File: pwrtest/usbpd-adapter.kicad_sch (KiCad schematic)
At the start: 30 parts, among them J1 Conn_01x04, J2 Conn_01x04, J3 USB_C_Receptacle_USB2.0_16P, Q1 AO3400A, U1 AP63205WU, U2 L7812, U3 IP2721

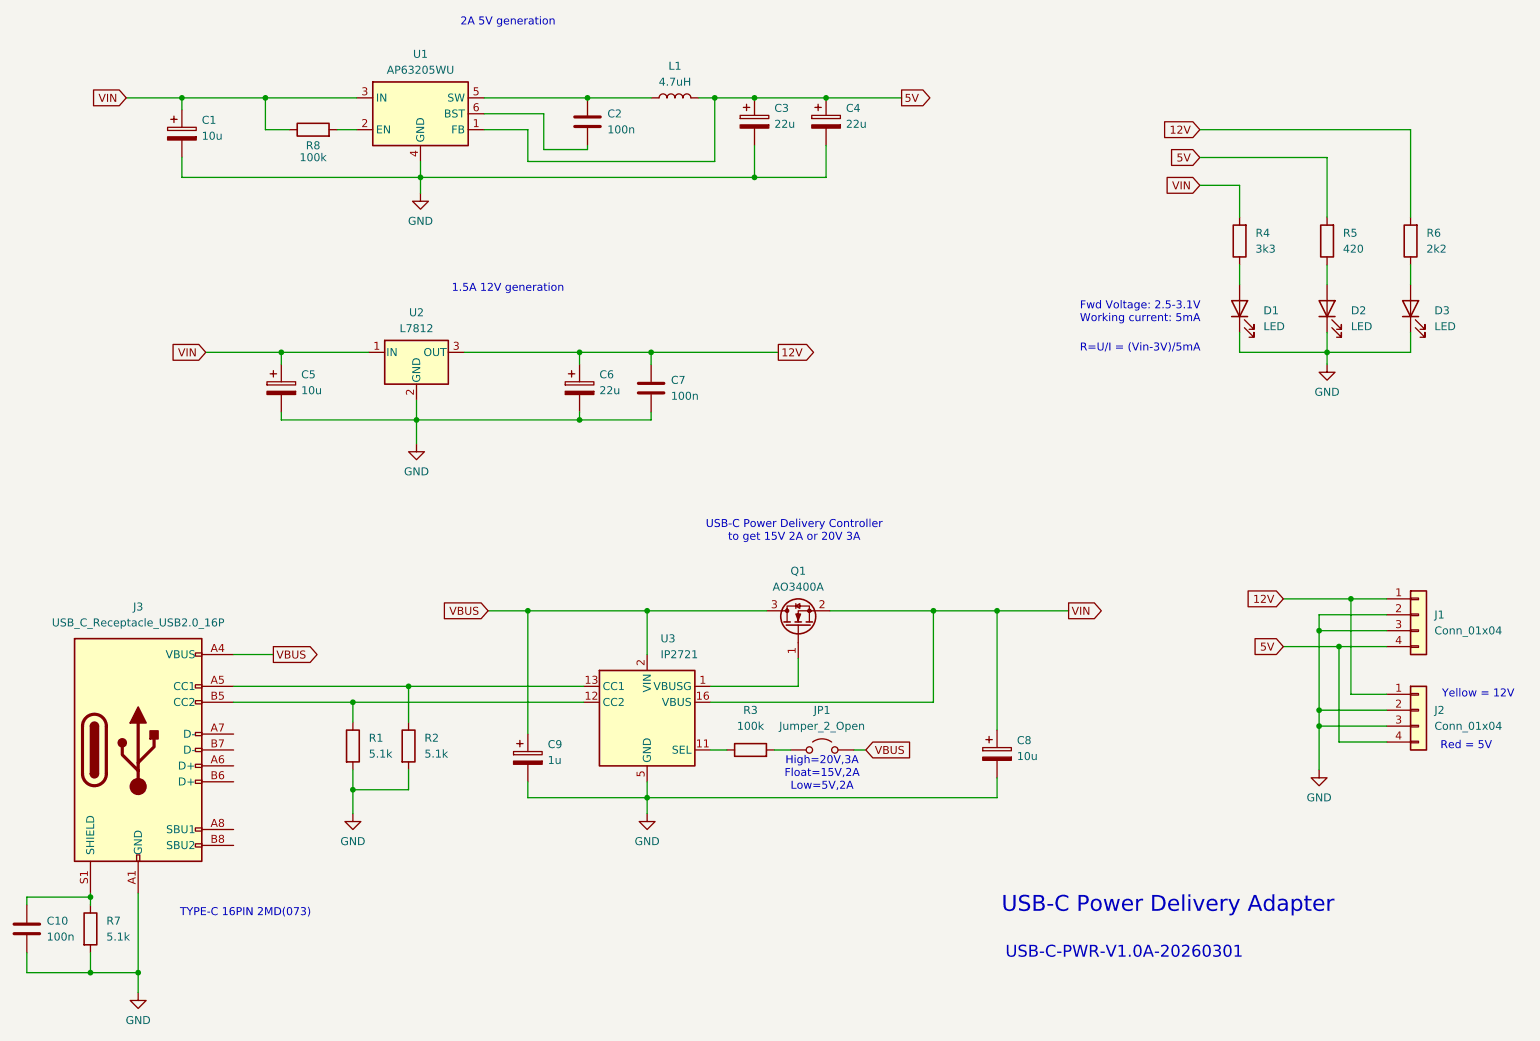
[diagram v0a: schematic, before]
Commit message: usb power adapter 1.1a
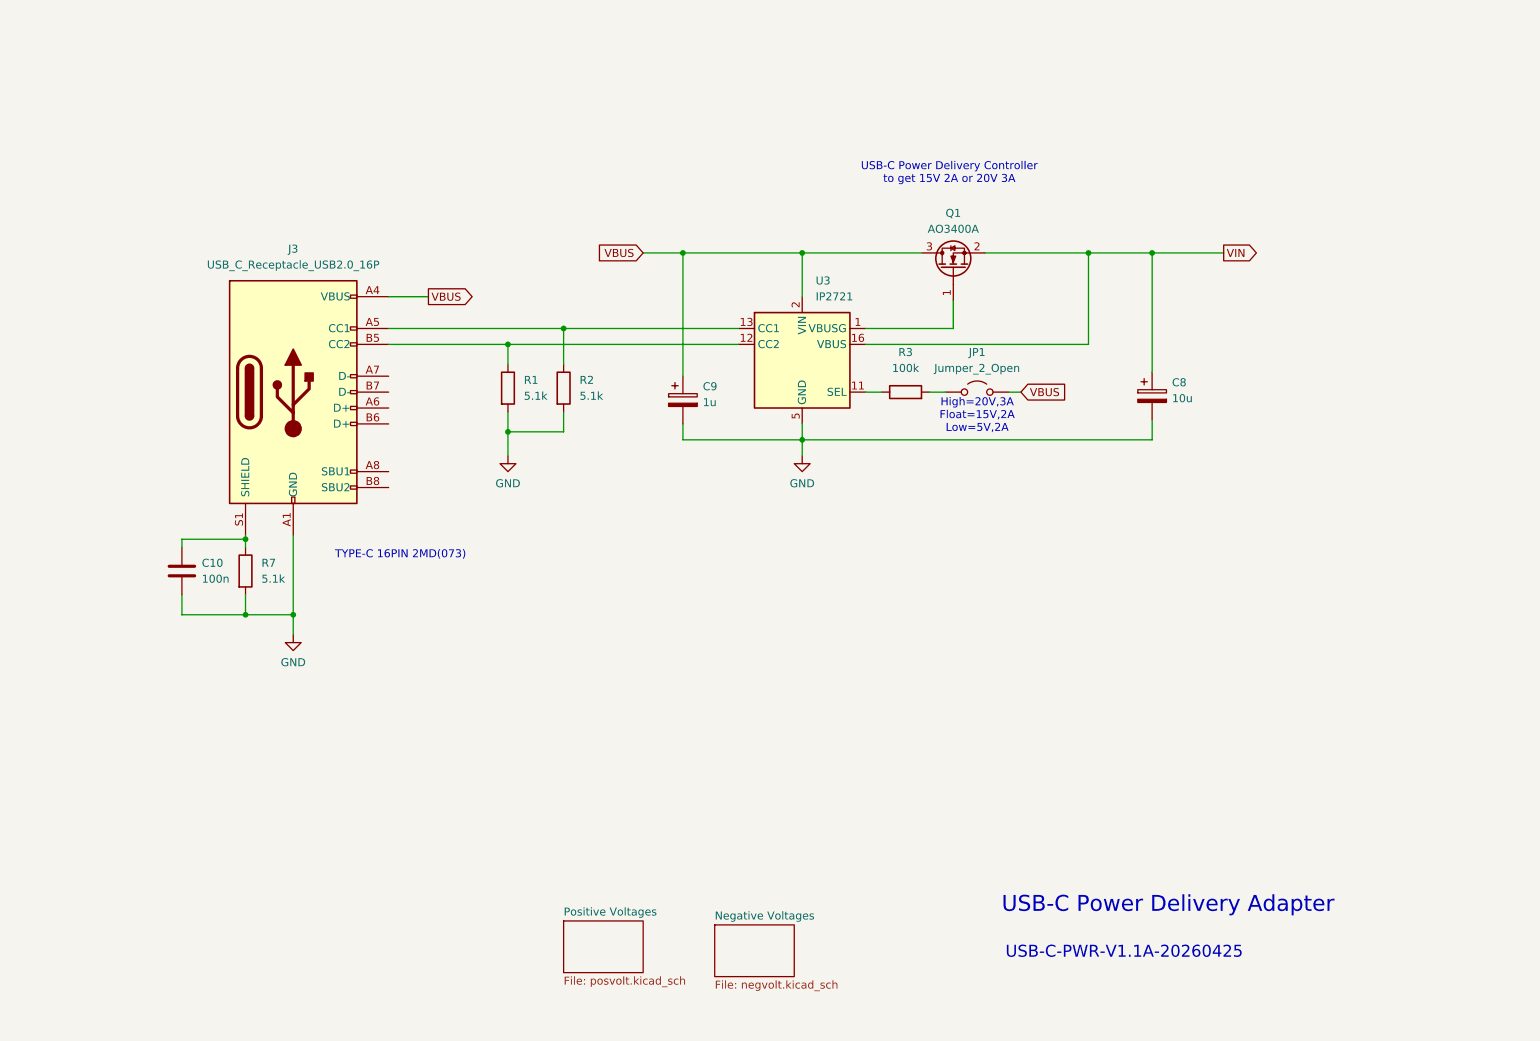
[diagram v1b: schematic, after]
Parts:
- removed C1, C5: 10u, Capacitor_SMD:C_1206_3216Metric_Pad1.33x1.80mm_HandSolder, symbol Device:C_Polarized
- removed C2, C7: 100n, Capacitor_SMD:C_0603_1608Metric_Pad1.08x0.95mm_HandSolder, symbol Device:C
- removed C3, C4, C6: 22u, Capacitor_SMD:C_1206_3216Metric_Pad1.33x1.80mm_HandSolder, symbol Device:C_Polarized
- removed D1, D2, D3: LED, Diode_SMD:D_0603_1608Metric_Pad1.05x0.95mm_HandSolder, symbol Device:LED
- removed J1: Conn_01x04, Connector_TE-Connectivity:TE_MATE-N-LOK_350211-1_1x04_P5.08mm_Vertical, symbol Connector_Generic:Conn_01x04
- removed J2: Conn_01x04, Connector_Samtec_HPM_THT:Samtec_HPM-04-05-x-S_Straight_1x04_Pitch5.08mm, symbol Connector_Generic:Conn_01x04
- removed L1: 4.7uH, Inductor_SMD:L_APV_ANR4030, symbol Device:L
- removed R4: 3k3, Resistor_SMD:R_0603_1608Metric_Pad0.98x0.95mm_HandSolder, symbol Device:R
- removed R5: 420, Resistor_SMD:R_0603_1608Metric_Pad0.98x0.95mm_HandSolder, symbol Device:R
- removed R6: 2k2, Resistor_SMD:R_0603_1608Metric_Pad0.98x0.95mm_HandSolder, symbol Device:R
- removed R8: 100k, Resistor_SMD:R_0603_1608Metric_Pad0.98x0.95mm_HandSolder, symbol Device:R
- removed U1: AP63205WU, Package_TO_SOT_SMD:TSOT-23-6, symbol Regulator_Switching:AP63205WU
- removed U2: L7812, Package_TO_SOT_THT:TO-220-3_Horizontal_TabDown, symbol Regulator_Linear:L7812
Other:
- added sheet Negative Voltages (negvolt.kicad_sch)
- added sheet Positive Voltages (posvolt.kicad_sch)
- note added: "USB-C-PWR-V1.1A-20260425"
- note removed: "1.5A 12V generation"
- note removed: "2A 5V generation"
- note removed: "Fwd Voltage: 2.5-3.1V Working current: 5mA"
- note removed: "R=U/I = (Vin-3V)/5mA"
- note removed: "Red = 5V"
- note removed: "USB-C-PWR-V1.0A-20260301"
- note removed: "Yellow = 12V"
- moved on the sheet: C10, C8, C9, J3, JP1, Q1, R1, R2, R3, R7, U3
